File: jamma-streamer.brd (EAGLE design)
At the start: 180.3 x 92 mm, 16 parts, among them J1 Audio line out, J3 SDCARD, U2 LM3940IMP-3.3/NOPB, U3 74HC4050D

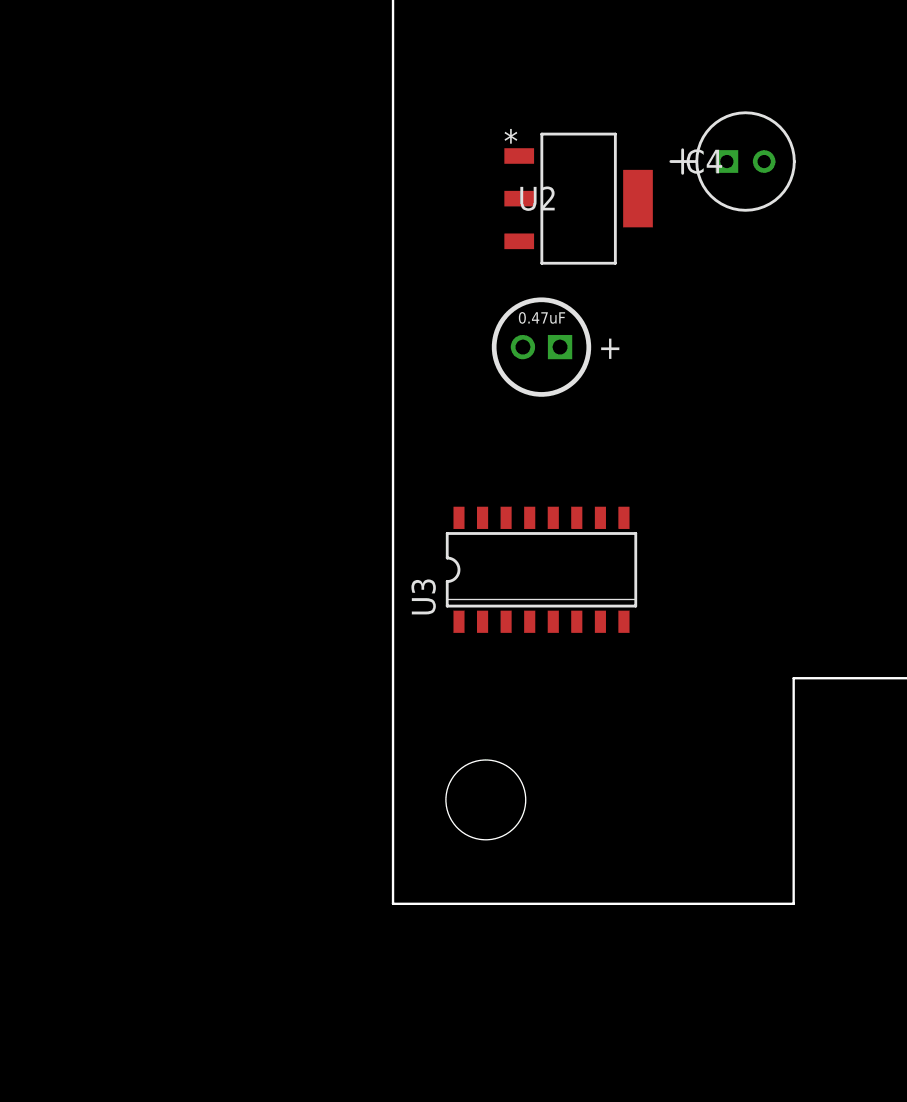
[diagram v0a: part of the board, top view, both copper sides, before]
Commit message: Added Micro SDCARD circuitry
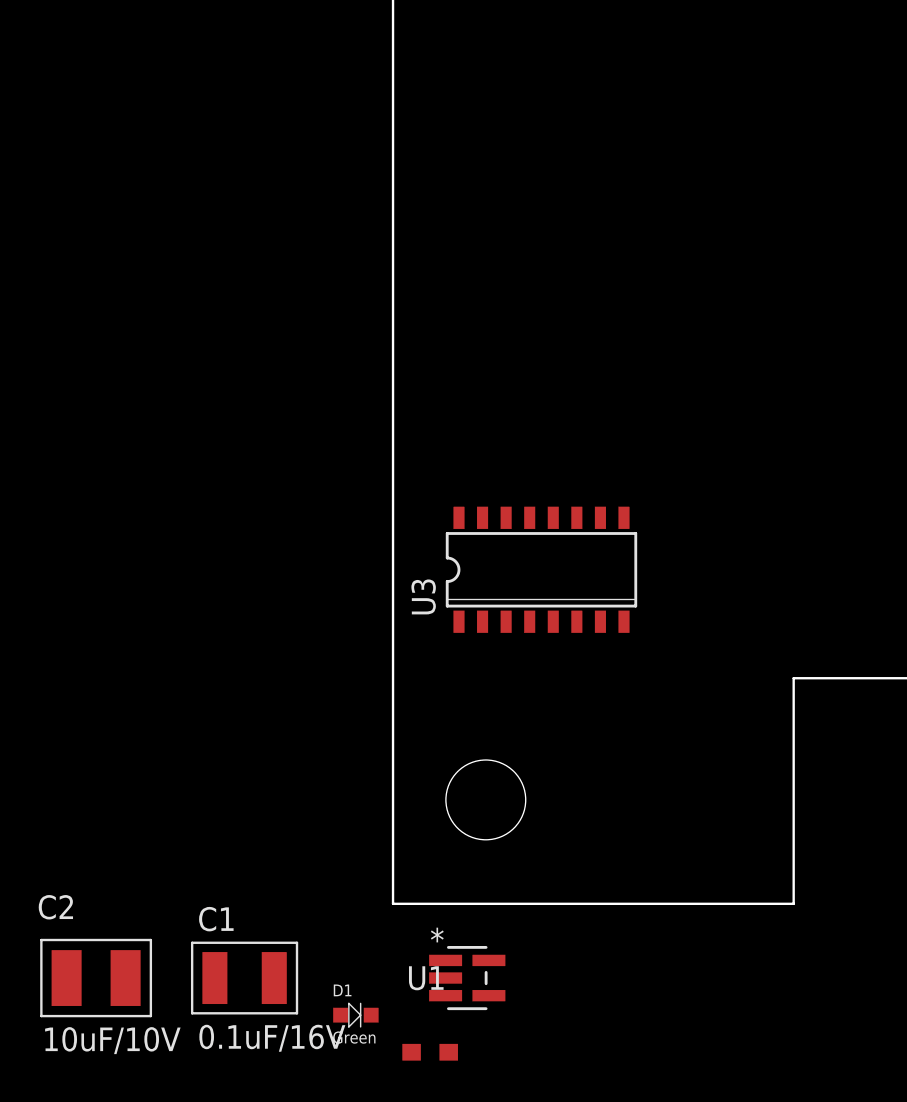
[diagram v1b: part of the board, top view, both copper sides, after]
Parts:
- removed C3: 0.47uF, capacitors:CAPACITOR_WE_0.47UF
- removed C4: 33uF, capacitors:U1-E
- removed U2: LM3940IMP-3.3/NOPB, LM3940:MP04A
- added C1: 0.1uF/16V, CMS:KEMET-C1210C104K4J
- added C2: 10uF/10V, CMS:C1210C106K8N
- added D1: Green, CMS:604-APTD1608LCGCK
- added R1: 1K, CMS:652-CHP0603FX1001ELF
- added U1: LP298X, LP2981-33DBVR:DBV5-M
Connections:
- removed net SCLK: J3.5
- new net CLK: U3.5, U3.9
- new net N$14: J3.2, R1.2, U3.6
- new net N$15: J3.3, U3.2
- new net N$17: J3.5, U3.4
- new net N$18: D1.+, U3.10
- new net N$19: D1.-, R1.1
- net +3.3V: now also C2.2, U1.5; no longer C4.1, U2.3
- net +5V: now also C1.2, U1.1, U1.3; no longer C3.+, U2.1
- net CS: now also U3.7; no longer J3.2
- net DI: now also U3.3; no longer J3.3
- net GND: now also C1.1, C2.1, U1.2, U3.11, U3.12, U3.14, U3.15; no longer C3.-, C4.2, U2.2, U2.4
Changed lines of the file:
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@@
 <attribute name="VALUE" x="160.56" y="51.306" size="0.6096" layer="27"/>
-</element>
-<element name="U2" library="LM3940" package="MP04A" value="LM3940IMP-3.3/NOPB" x="10" y="38" smashed="yes">
-<attribute name="MANUFACTURER_PART_NUMBER" value="LM3940IMP3.3NOPB" x="10" y="58" size="1.778" layer="27" display="off"/>
-<attribute name="NAME" x="6.7234" y="37.365" size="1.27" layer="25" ratio="6" rot="SR0"/>
-<attribute name="VENDOR" value="Texas Instruments" x="10" y="58" size="1.778" layer="27" display="off"/>
-</element>
-<element name="C3" library="capacitors" package="CAPACITOR_WE_0.47UF" value="0.47uF" x="8" y="30" smashed="yes">
-<attribute name="VALUE" x="6.73" y="31.27" size="0.6096" layer="21"/>
-</element>
-<element name="C4" library="capacitors" package="U1-E" value="33uF" x="20" y="40" smashed="yes">
-<attribute name="MANUFACTURER_PART_NUMBER" value="UKA1C330MDD1TD" x="10" y="44" size="1.778" layer="27" display="off"/>
-<attribute name="NAME" x="15.7328" y="39.365" size="1.27" layer="25" ratio="6" rot="SR0"/>
-<attribute name="VENDOR" value="Nichicon" x="10" y="44" size="1.778" layer="27" display="off"/>
 </element>
 <element name="J3" library="DM3CS-SF" package="HRS_DM3CS-SF" value="SDCARD" x="12" y="72" smashed="yes" rot="R90">
@@
 <attribute name="PACKAGE" value="SOIC-16 Toshiba" x="8" y="18" size="1.778" layer="27" display="off"/>
 <attribute name="PRICE" value="None" x="8" y="18" size="1.778" layer="27" display="off"/>
+</element>
+<element name="U1" library="LP2981-33DBVR" package="DBV5-M" value="LP298X" x="4" y="-4" smashed="yes">
+<attribute name="MANUFACTURER_PART_NUMBER" value="LP298133DBVR" x="4" y="-4" size="1.778" layer="27" display="off"/>
+<attribute name="NAME" x="0.7234" y="-4.635" size="1.27" layer="25" ratio="6" rot="SR0"/>
+<attribute name="VENDOR" value="Texas Instruments" x="4" y="-4" size="1.778" layer="27" display="off"/>
+</element>
+<element name="R1" library="CMS" package="652-CHP0603FX1001ELF" value="1K" x="2" y="-8" smashed="yes"/>
+<element name="D1" library="CMS" package="604-APTD1608LCGCK" value="Green" x="-2" y="-6" smashed="yes">
+<attribute name="NAME" x="-3.27" y="-4.984" size="0.635" layer="21"/>
+<attribute name="VALUE" x="-3.27" y="-7.524" size="0.635" layer="21"/>
+</element>
+<element name="C1" library="CMS" package="KEMET-C1210C104K4J" value="0.1uF/16V" x="-8" y="-4" smashed="yes">
+<attribute name="NAME" x="-10.54" y="-1.46" size="1.27" layer="21"/>
+<attribute name="VALUE" x="-10.54" y="-7.81" size="1.27" layer="21"/>
+</element>
+<element name="C2" library="CMS" package="C1210C106K8N" value="10uF/10V" x="-16" y="-4" smashed="yes">
+<attribute name="NAME" x="-19.18" y="-0.82" size="1.27" layer="21"/>
+<attribute name="VALUE" x="-18.921" y="-7.937" size="1.27" layer="21"/>
 </element>
 </elements>
@@
 <wire x1="143.067" y1="84.547" x2="143.067" y2="12.6" width="0.508" layer="16"/>
 <wire x1="143.067" y1="12.6" x2="141.9" y2="12.6" width="0.508" layer="16"/>
-<contactref element="U2" pad="4"/>
-<contactref element="U2" pad="2"/>
-<contactref element="C3" pad="-"/>
-<contactref element="C4" pad="2"/>
 <contactref element="J3" pad="S1"/>
 <contactref element="J3" pad="S5"/>
@@
 <contactref element="J3" pad="1"/>
 <contactref element="U3" pad="8"/>
-<wire x1="18.35" y1="75.2" x2="17.85" y2="78.75" width="0" layer="19" extent="1-1"/>
-<wire x1="18.35" y1="69.7" x2="18.35" y2="75.2" width="0" layer="19" extent="1-1"/>
-<wire x1="18.35" y1="67.5" x2="18.35" y2="69.7" width="0" layer="19" extent="1-1"/>
-<wire x1="17.85" y1="65.4" x2="18.35" y2="67.5" width="0" layer="19" extent="1-1"/>
+<contactref element="U1" pad="2"/>
+<contactref element="U3" pad="11"/>
+<contactref element="U3" pad="14"/>
+<contactref element="U3" pad="12"/>
+<contactref element="U3" pad="15"/>
+<contactref element="C1" pad="1"/>
+<contactref element="C2" pad="1"/>
+<wire x1="143.051" y1="6.166" x2="143.051" y2="6.166" width="0" layer="19" extent="1-16"/>
+<wire x1="36.131" y1="6.166" x2="36.131" y2="6.166" width="0" layer="19" extent="1-16"/>
+<wire x1="140.1" y1="12.6" x2="141.9" y2="12.6" width="0" layer="19" extent="1-1"/>
+<wire x1="139.091" y1="6.166" x2="139.091" y2="6.166" width="0" layer="19" extent="1-16"/>
+<wire x1="39.3" y1="12.6" x2="36.9" y2="12.6" width="0" layer="19" extent="16-16"/>
+<wire x1="40.091" y1="6.166" x2="40.091" y2="6.166" width="0" layer="19" extent="1-16"/>
+<wire x1="17.85" y1="65.4" x2="35.82" y2="60.3" width="0" layer="19" extent="1-16"/>
+<wire x1="18.35" y1="67.5" x2="17.85" y2="65.4" width="0" layer="19" extent="1-1"/>
+<wire x1="18.35" y1="69.7" x2="18.35" y2="67.5" width="0" layer="19" extent="1-1"/>
+<wire x1="18.35" y1="75.2" x2="18.35" y2="69.7" width="0" layer="19" extent="1-1"/>
+<wire x1="17.85" y1="78.75" x2="18.35" y2="75.2" width="0" layer="19" extent="1-1"/>
 <wire x1="5.55" y1="76.85" x2="17.85" y2="78.75" width="0" layer="19" extent="1-1"/>
 <wire x1="5.65" y1="68.9" x2="5.55" y2="76.85" width="0" layer="19" extent="1-1"/>
-<wire x1="35.82" y1="60.3" x2="17.85" y2="65.4" width="0" layer="19" extent="1-16"/>
-<wire x1="20" y1="40" x2="17.85" y2="65.4" width="0" layer="19" extent="1-1"/>
-<wire x1="13.2004" y1="38" x2="20" y2="40" width="0" layer="19" extent="1-1"/>
-<wire x1="6.7996" y1="38" x2="13.2004" y2="38" width="0" layer="19" extent="1-1"/>
-<wire x1="7" y1="30" x2="6.7996" y2="38" width="0" layer="19" extent="1-1"/>
-<wire x1="12.445" y1="15.2" x2="36.131" y2="6.166" width="0" layer="19" extent="1-1"/>
+<wire x1="12.445" y1="15.2" x2="35.82" y2="12.6" width="0" layer="19" extent="1-16"/>
+<wire x1="9.905" y1="20.8" x2="12.445" y2="15.2" width="0" layer="19" extent="1-1"/>
+<wire x1="8.635" y1="20.8" x2="9.905" y2="20.8" width="0" layer="19" extent="1-1"/>
+<wire x1="6.095" y1="20.8" x2="8.635" y2="20.8" width="0" layer="19" extent="1-1"/>
+<wire x1="4.825" y1="20.8" x2="6.095" y2="20.8" width="0" layer="19" extent="1-1"/>
+<wire x1="2.8316" y1="-4" x2="12.445" y2="15.2" width="0" layer="19" extent="1-1"/>
+<wire x1="-9.6" y1="-4" x2="2.8316" y2="-4" width="0" layer="19" extent="1-1"/>
+<wire x1="-17.59" y1="-4" x2="-9.6" y2="-4" width="0" layer="19" extent="1-1"/>
 </signal>
 <signal name="VGROUND">
@@
 <wire x1="44.067" y1="84.547" x2="44.067" y2="13.533" width="0.4" layer="16"/>
 <wire x1="44.067" y1="13.533" x2="45" y2="12.6" width="0.4" layer="16"/>
-<contactref element="C3" pad="+"/>
-<contactref element="U2" pad="1"/>
-<wire x1="6.7996" y1="40.3" x2="9" y2="30" width="0" layer="19" extent="1-1"/>
-<wire x1="44.051" y1="6.166" x2="6.7996" y2="40.3" width="0" layer="19" extent="1-1"/>
+<contactref element="U1" pad="1"/>
+<contactref element="U1" pad="3"/>
+<contactref element="C1" pad="2"/>
+<wire x1="48.011" y1="6.166" x2="48.011" y2="6.166" width="0" layer="19" extent="1-16"/>
+<wire x1="45" y1="12.6" x2="47.1" y2="12.6" width="0" layer="19" extent="16-16"/>
+<wire x1="44.051" y1="6.166" x2="44.051" y2="6.166" width="0" layer="19" extent="1-16"/>
+<wire x1="2.8316" y1="-3.05" x2="44.051" y2="6.166" width="0" layer="19" extent="1-1"/>
+<wire x1="2.8316" y1="-4.95" x2="2.8316" y2="-3.05" width="0" layer="19" extent="1-1"/>
+<wire x1="-6.4" y1="-4" x2="2.8316" y2="-3.05" width="0" layer="19" extent="1-1"/>
 </signal>
 <signal name="+3.3V">
-<contactref element="C4" pad="1"/>
-<contactref element="U2" pad="3"/>
 <contactref element="J3" pad="4"/>
 <contactref element="U3" pad="1"/>
-<wire x1="17.9934" y1="40" x2="18.35" y2="71.9" width="0" layer="19" extent="1-1"/>
-<wire x1="6.7996" y1="35.7" x2="17.9934" y2="40" width="0" layer="19" extent="1-1"/>
-<wire x1="3.555" y1="15.2" x2="6.7996" y2="35.7" width="0" layer="19" extent="1-1"/>
-</signal>
-<signal name="CS">
-<contactref element="J3" pad="2"/>
-</signal>
-<signal name="DI">
-<contactref element="J3" pad="3"/>
-</signal>
-<signal name="SCLK">
-<contactref element="J3" pad="5"/>
+<contactref element="U1" pad="5"/>
+<contactref element="C2" pad="2"/>
+<wire x1="3.555" y1="15.2" x2="18.35" y2="71.9" width="0" layer="19" extent="1-1"/>
+<wire x1="5.1684" y1="-3.05" x2="3.555" y2="15.2" width="0" layer="19" extent="1-1"/>
+<wire x1="-14.41" y1="-4" x2="5.1684" y2="-3.05" width="0" layer="19" extent="1-1"/>
 </signal>
 <signal name="DO">
 <contactref element="J3" pad="7"/>
 </signal>
+<signal name="DI">
+<contactref element="U3" pad="3"/>
+</signal>
+<signal name="N$15">
+<contactref element="U3" pad="2"/>
+<contactref element="J3" pad="3"/>
+<wire x1="4.825" y1="15.2" x2="18.35" y2="73" width="0" layer="19" extent="1-1"/>
+</signal>
+<signal name="CLK">
+<contactref element="U3" pad="5"/>
+<contactref element="U3" pad="9"/>
+<wire x1="8.635" y1="15.2" x2="12.445" y2="20.8" width="0" layer="19" extent="1-1"/>
+</signal>
+<signal name="N$17">
+<contactref element="U3" pad="4"/>
+<contactref element="J3" pad="5"/>
+<wire x1="7.365" y1="15.2" x2="18.35" y2="70.8" width="0" layer="19" extent="1-1"/>
+</signal>
+<signal name="N$14">
+<contactref element="J3" pad="2"/>
+<contactref element="U3" pad="6"/>
+<contactref element="R1" pad="2"/>
+<wire x1="9.905" y1="15.2" x2="18.35" y2="74.1" width="0" layer="19" extent="1-1"/>
+<wire x1="3" y1="-8" x2="9.905" y2="15.2" width="0" layer="19" extent="1-1"/>
+</signal>
+<signal name="CS">
+<contactref element="U3" pad="7"/>
+</signal>
+<signal name="N$18">
+<contactref element="U3" pad="10"/>
+<contactref element="D1" pad="+"/>
+<wire x1="-2.825" y1="-6" x2="11.175" y2="20.8" width="0" layer="19" extent="1-1"/>
+</signal>
+<signal name="N$19">
+<contactref element="D1" pad="-"/>
+<contactref element="R1" pad="1"/>
+<wire x1="-1.175" y1="-6" x2="1" y2="-8" width="0" layer="19" extent="1-1"/>
+</signal>
 </signals>

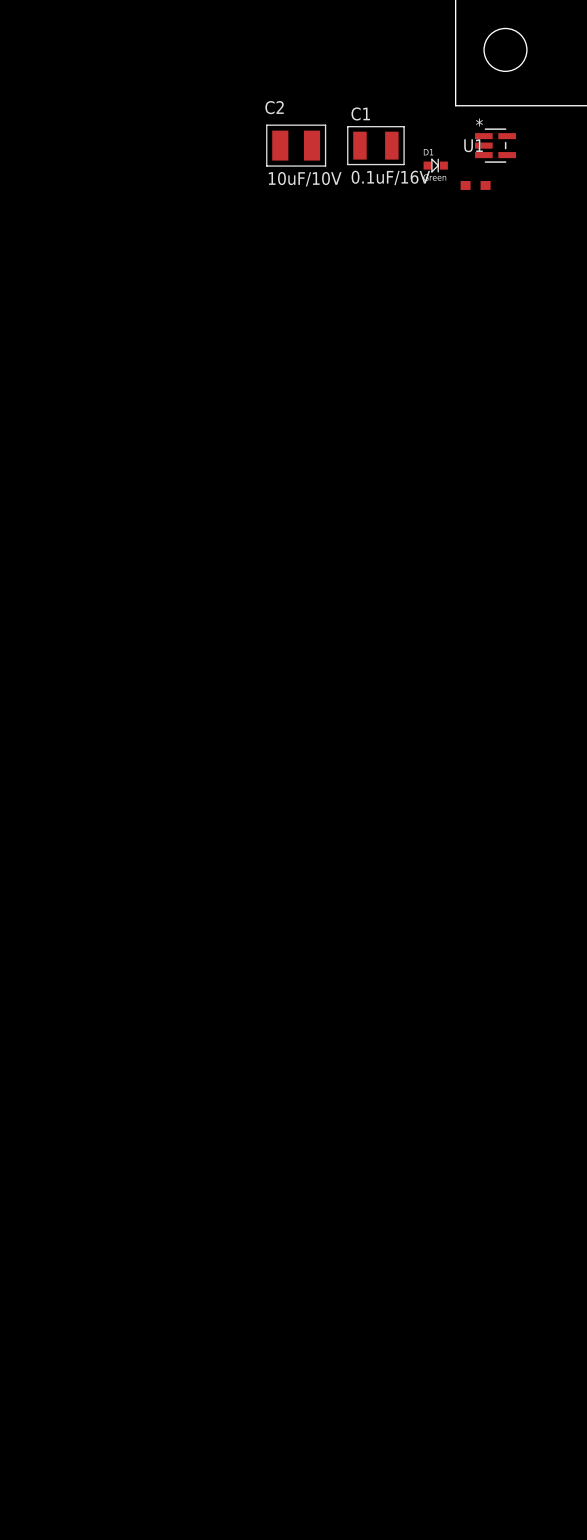
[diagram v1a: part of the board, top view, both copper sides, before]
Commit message: Added atmega328p and begining wiring
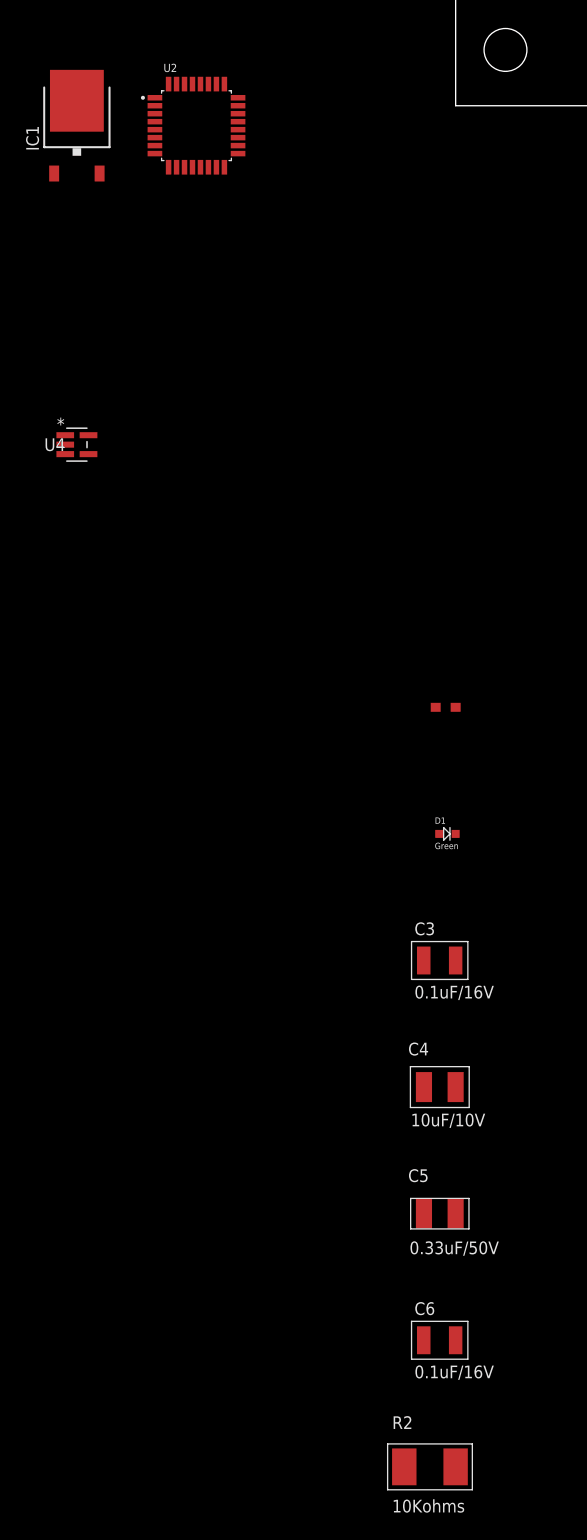
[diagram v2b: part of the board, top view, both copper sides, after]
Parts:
- removed C1: 0.1uF/16V, CMS:KEMET-C1210C104K4J
- removed C2: 10uF/10V, CMS:C1210C106K8N
- removed U1: LP298X, LP2981-33DBVR:DBV5-M
- added C3, C6: 0.1uF/16V, CMS:KEMET-C1210C104K4J
- added C4: 10uF/10V, CMS:KEMET-C1210C106K8N
- added C5: 0.33uF/50V, CMS:KEMET-C1206X334K5R
- added IC1: LM7805, linear:TO252
- added R2: 10Kohms, CMS:BOURNS-CRM2512AJW-103ELF
- added U2: ATMEGA328PB-AUR, ATMEGA328PB-AUR:QFP80P900X900X120-32N
- added U4: LP298X, LP2981-33DBVR:DBV5-M
- moved D1 67.1 mm to (-0.82, -73.0)
- moved R1 52.4 mm to (-1.00, -60.4)
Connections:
- net -5V renamed JAMMA-5V
- removed net +12V: JAMMA_IN.6, JAMMA_IN.F, JAMMA_OUT_BTM.F, JAMMA_OUT_TOP.6
- removed net +3.3V: C2.2, J3.4, U1.5, U3.1
- removed net +5V: C1.2, JAMMA_IN.3, JAMMA_IN.4, JAMMA_IN.C, JAMMA_IN.D, JAMMA_OUT_BTM.C, JAMMA_OUT_BTM.D, JAMMA_OUT_TOP.3, JAMMA_OUT_TOP.4, U1.1, U1.3
- new net AVCC: U2.18
- new net JAMMA+12V: C5.1, IC1.1, JAMMA_IN.6, JAMMA_IN.F, JAMMA_OUT_BTM.F, JAMMA_OUT_TOP.6
- new net JAMMA+5V: JAMMA_IN.3, JAMMA_IN.4, JAMMA_IN.C, JAMMA_IN.D, JAMMA_OUT_BTM.C, JAMMA_OUT_BTM.D, JAMMA_OUT_TOP.3, JAMMA_OUT_TOP.4
- new net N$9: R2.2, U2.29
- new net VCC: C3.2, C6.1, IC1.2, R2.1, U2.4, U4.1, U4.3
- new net VCC_2: C4.2, J3.4, U3.1, U4.5
- net GND: now also C3.1, C4.1, C5.2, C6.2, IC1.3, U2.21, U2.5, U4.2; no longer C1.1, C2.1, U1.2
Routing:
- net JAMMA+5V: track 0.00 -> 100.2 mm, vias 0 -> 2
- net +5V: track 100.2 -> 0.00 mm, vias 2 -> 0
- net JAMMA+12V: track 0.00 -> 90.6 mm, vias 0 -> 1
- net +12V: track 90.6 -> 0.00 mm, vias 1 -> 0
- added copper zone on layer 16, net JAMMA+5V
- removed copper zone on layer 16, net +5V
